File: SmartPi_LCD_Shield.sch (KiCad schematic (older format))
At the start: 54 parts, among them J1 Ant_SMA, J2 Conn_01x01, J3 Micro_SD_Card, J4 Conn_01x02, J5 Conn_01x16, Q1 BC547, SW1 Reset, SW2 UP, SW3 LEFT, SW4 RIGHT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

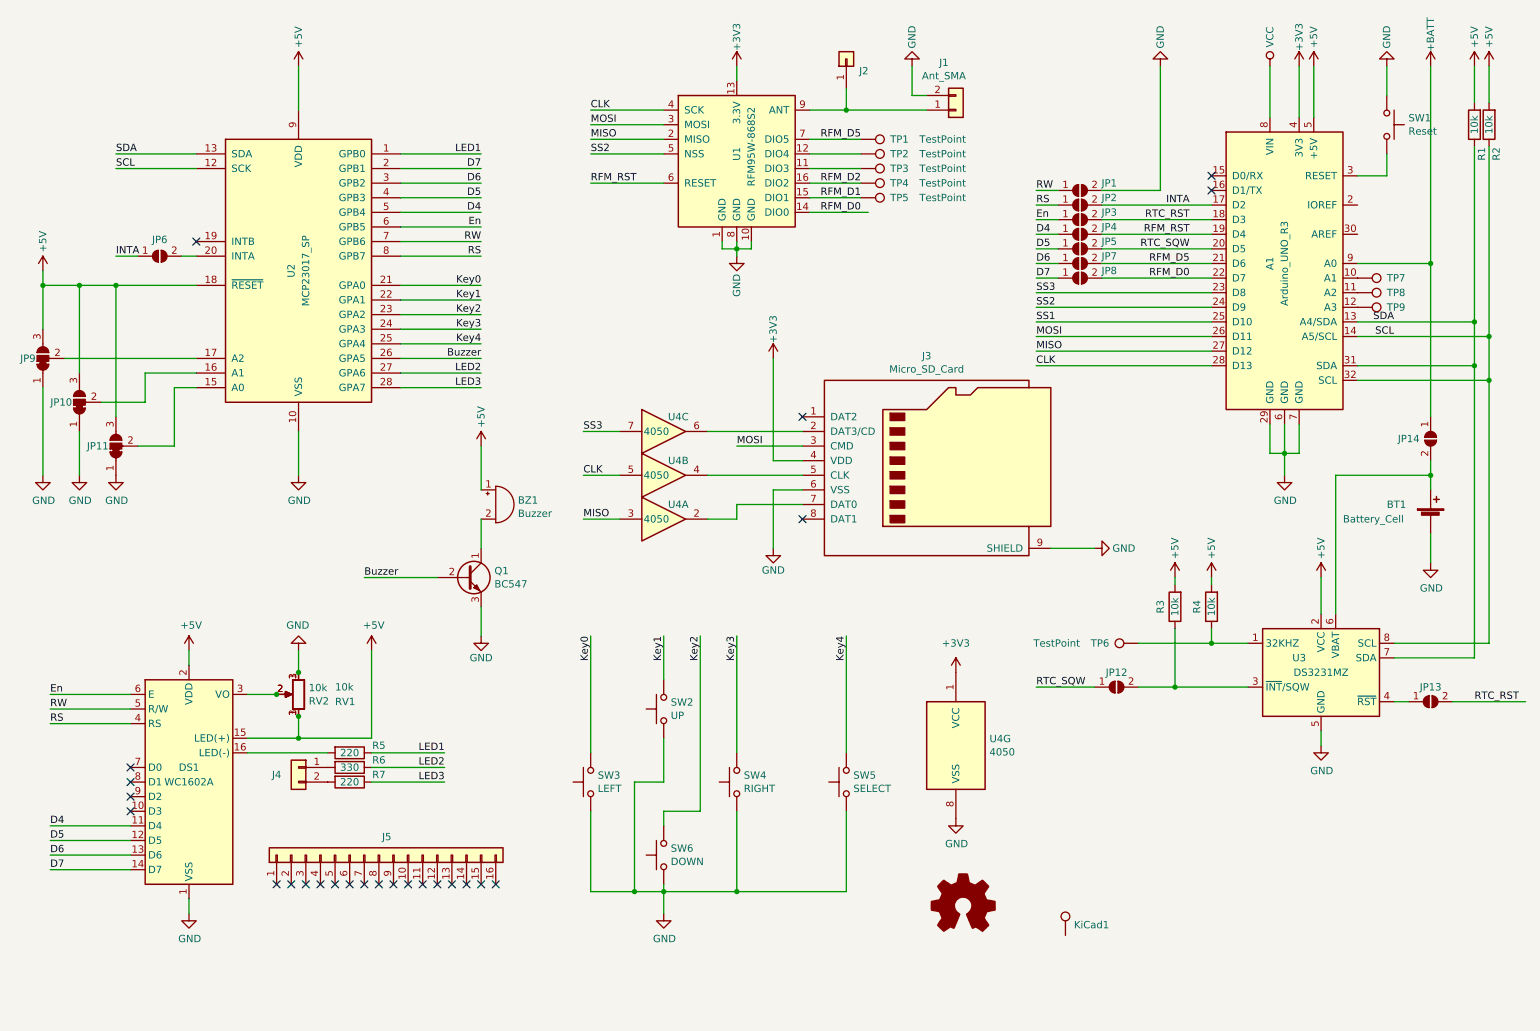
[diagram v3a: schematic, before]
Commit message: added option for analog buttons
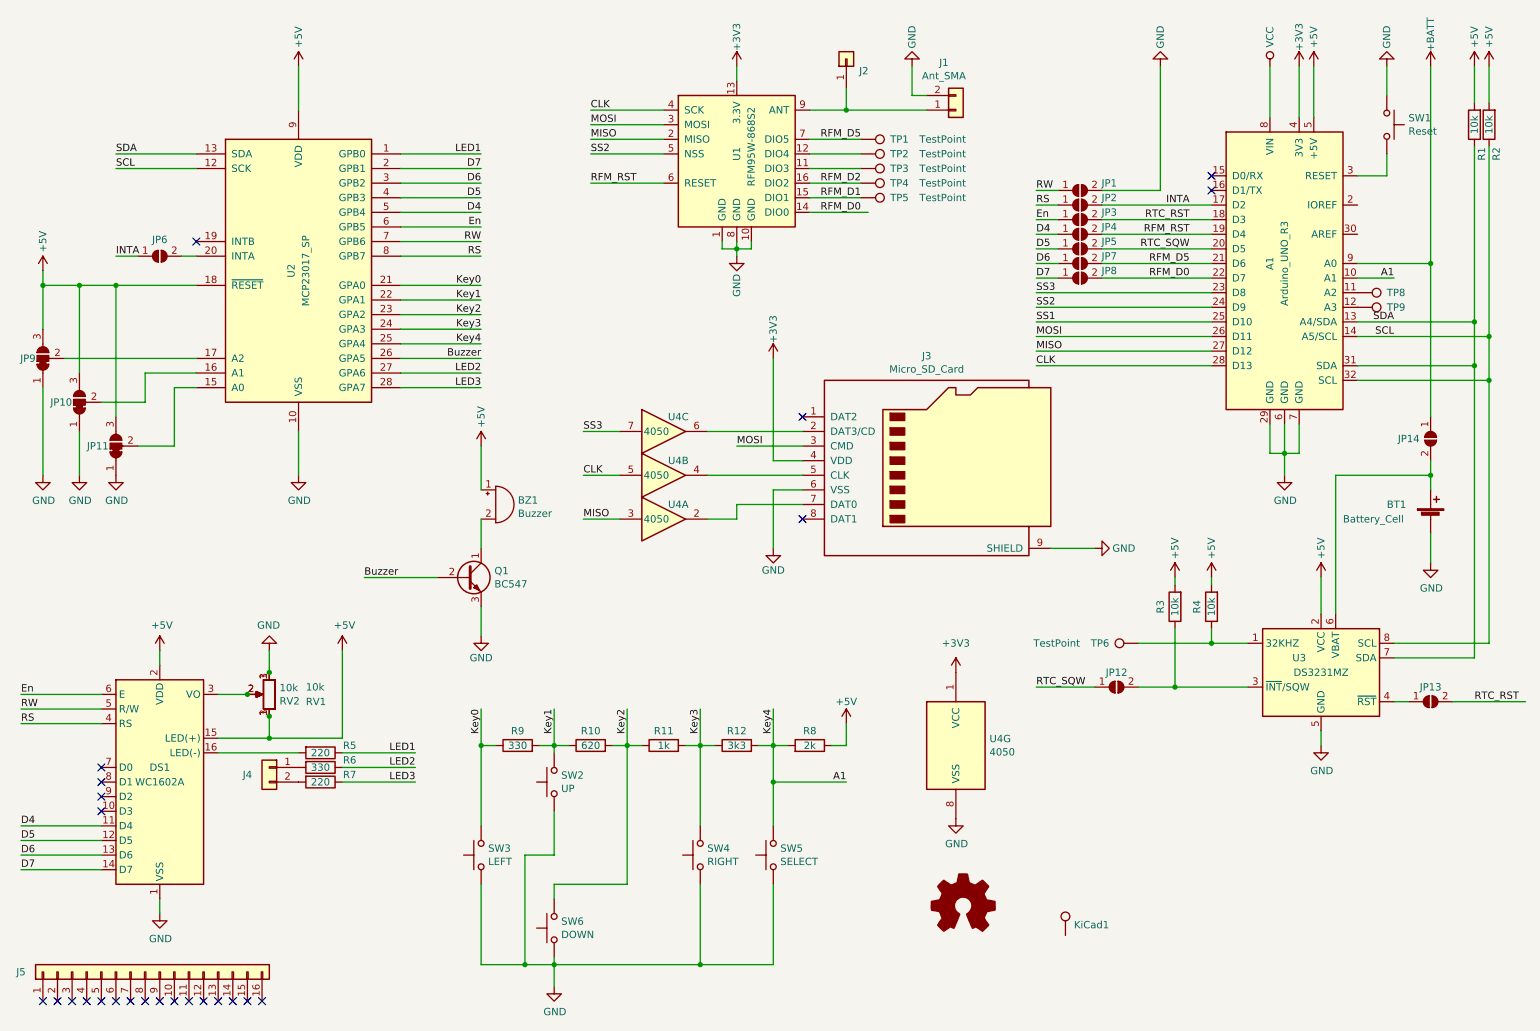
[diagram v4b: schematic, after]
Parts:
- removed TP7: TestPoint, TestPoint:TestPoint_Pad_D2.0mm, symbol Connector:TestPoint
- added R10: 620, Resistor_THT:R_Axial_DIN0204_L3.6mm_D1.6mm_P7.62mm_Horizontal, symbol Device:R
- added R11: 1k, Resistor_THT:R_Axial_DIN0204_L3.6mm_D1.6mm_P7.62mm_Horizontal, symbol Device:R
- added R12: 3k3, Resistor_THT:R_Axial_DIN0204_L3.6mm_D1.6mm_P7.62mm_Horizontal, symbol Device:R
- added R8: 2k, Resistor_THT:R_Axial_DIN0204_L3.6mm_D1.6mm_P7.62mm_Horizontal, symbol Device:R
- added R9: 330, Resistor_THT:R_Axial_DIN0204_L3.6mm_D1.6mm_P7.62mm_Horizontal, symbol Device:R
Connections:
- net Key4 is gone; now on net A1: SW5.2, U2.25 (GPA4)
- net +5V: now also R8.1
- net Key0: now also R9.1
- net Key1: now also R10.1, R9.2
- net Key2: now also R10.2, R11.1
- net Key3: now also R11.2, R12.1
- net A1: now reaches A1.10 (A1)
- net A1: now also R12.2, R8.2
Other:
- moved on the sheet: DS1, J4, J5, R5, R6, R7, RV1, RV2, SW2, SW3, SW4, SW5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

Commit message: new description
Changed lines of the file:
@@
 Wire Wire Line
 	6000 5750 6100 5750
+Text Label 10250 2450 2    50   ~ 0
+A0
 $EndSCHEMATC
